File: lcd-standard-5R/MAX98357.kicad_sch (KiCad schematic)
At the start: 5 parts, among them J7 Conn_01x02_MountingPin, U9 MAX98357A

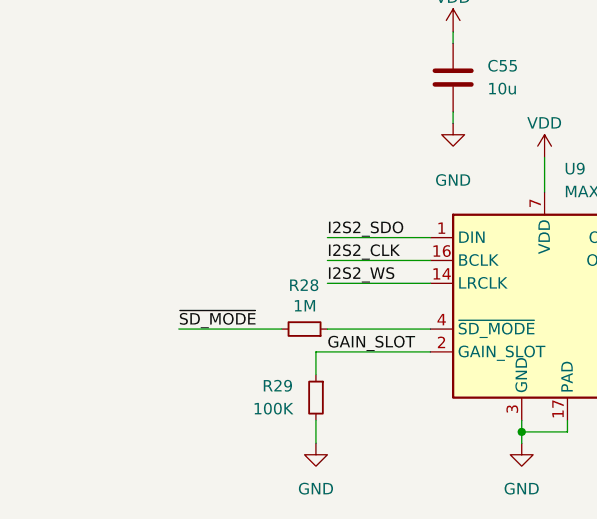
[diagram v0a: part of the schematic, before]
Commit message: Change MCU to STM32H743
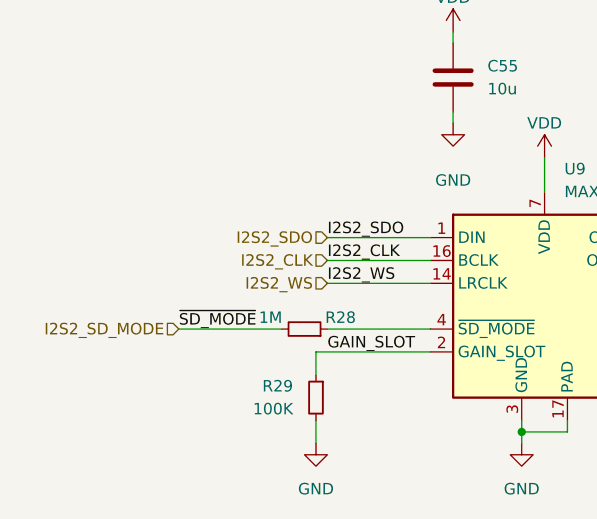
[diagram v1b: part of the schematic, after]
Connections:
- net ~{SD_MODE} renamed I2S2_SD_MODE
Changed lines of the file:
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@@
+		)
+	)
+	(hierarchical_label "I2S2_SD_MODE"
+		(shape input)
+		(at 100.33 105.41 180)
+		(fields_autoplaced yes)
+		(effects
+			(font
+				(size 1.27 1.27)
+			)
+			(justify right)
+		)
+	)
+	(hierarchical_label "I2S2_WS"
+		(shape input)
+		(at 116.84 100.33 180)
+		(fields_autoplaced yes)
+		(effects
+			(font
+				(size 1.27 1.27)
+			)
+			(justify right)
+		)
+	)
+	(hierarchical_label "I2S2_CLK"
+		(shape input)
+		(at 116.84 97.79 180)
+		(fields_autoplaced yes)
+		(effects
+			(font
+				(size 1.27 1.27)
+			)
+			(justify right)
+		)
+	)
+	(hierarchical_label "I2S2_SDO"
+		(shape input)
+		(at 116.84 95.25 180)
+		(fields_autoplaced yes)
+		(effects
+			(font
+				(size 1.27 1.27)
+			)
+			(justify right)
 		)
 	)
@@
 		(dnp no)
 		(property "Reference" "R28"
-			(at 112.522 100.584 90)
+			(at 116.586 104.14 90)
 			(effects
 				(font
@@
 		)
 		(property "Value" "1M"
-			(at 113.0301 102.87 90)
-			(effects
-				(font
+			(at 109.22 104.14 90)
+			(effects
+				(font

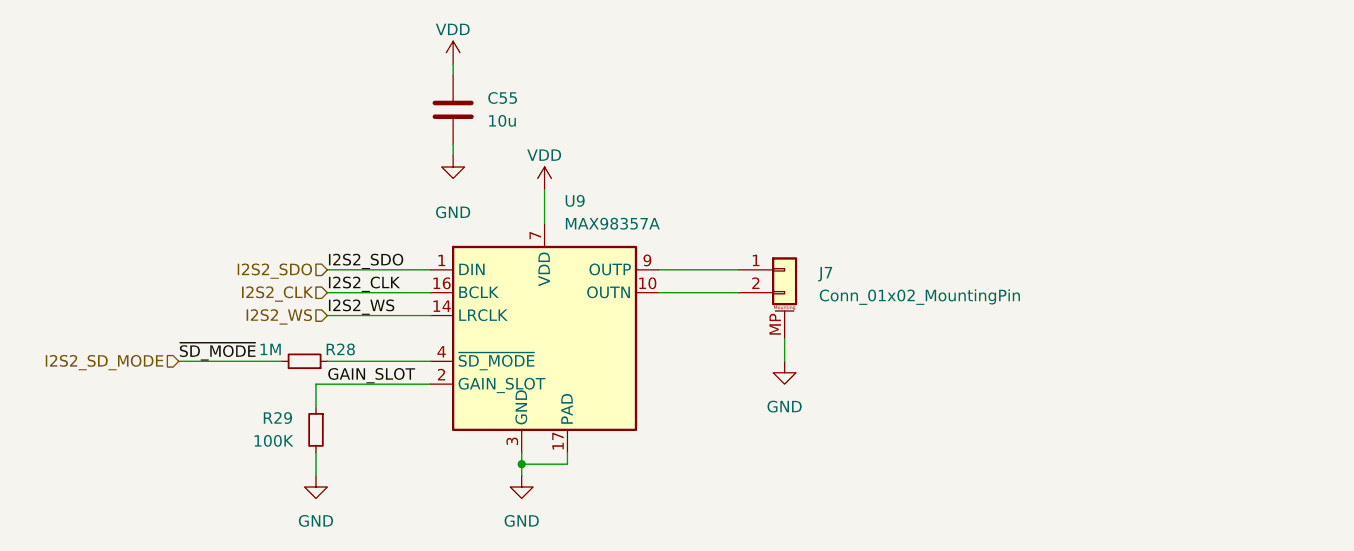
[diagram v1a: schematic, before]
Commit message: Adding filter on MAX98357, TODO: Add more grounding vias
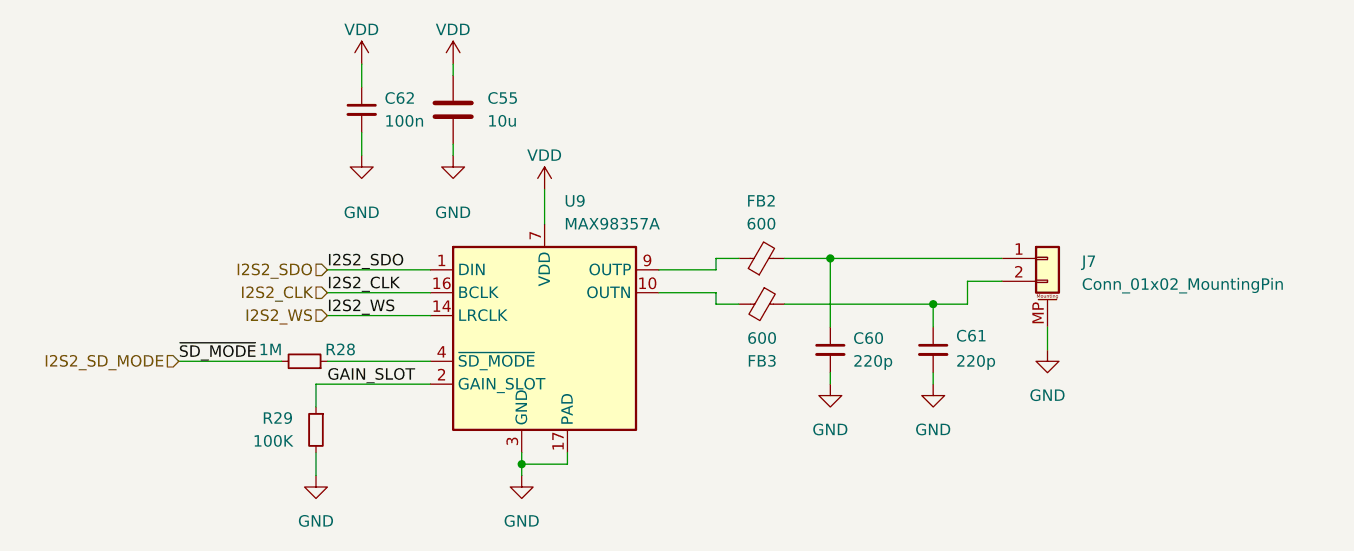
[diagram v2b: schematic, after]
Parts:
- added C60, C61: 220p, Capacitor_SMD:C_0805_2012Metric, symbol Device:C_Small
- added C62: 100n, Capacitor_SMD:C_0402_1005Metric, symbol Device:C_Small
- added FB2, FB3: 600, Inductor_SMD:L_0805_2012Metric, symbol Device:FerriteBead_Small
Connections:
- net GND: now also C60.2, C61.2, C62.2
- net VDD: now also C62.1
- net at U9.10 (OUTN): now also FB3.2; no longer J7.2 (Pin_2)
- net at J7.1 (Pin_1): now also C60.1, FB2.2; no longer U9.9 (OUTP)
- new net: FB2.1, U9.9 (OUTP)
- new net: C61.1, FB3.1, J7.2 (Pin_2)
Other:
- moved on the sheet: J7
